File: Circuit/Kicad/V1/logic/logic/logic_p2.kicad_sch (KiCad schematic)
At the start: 2 parts

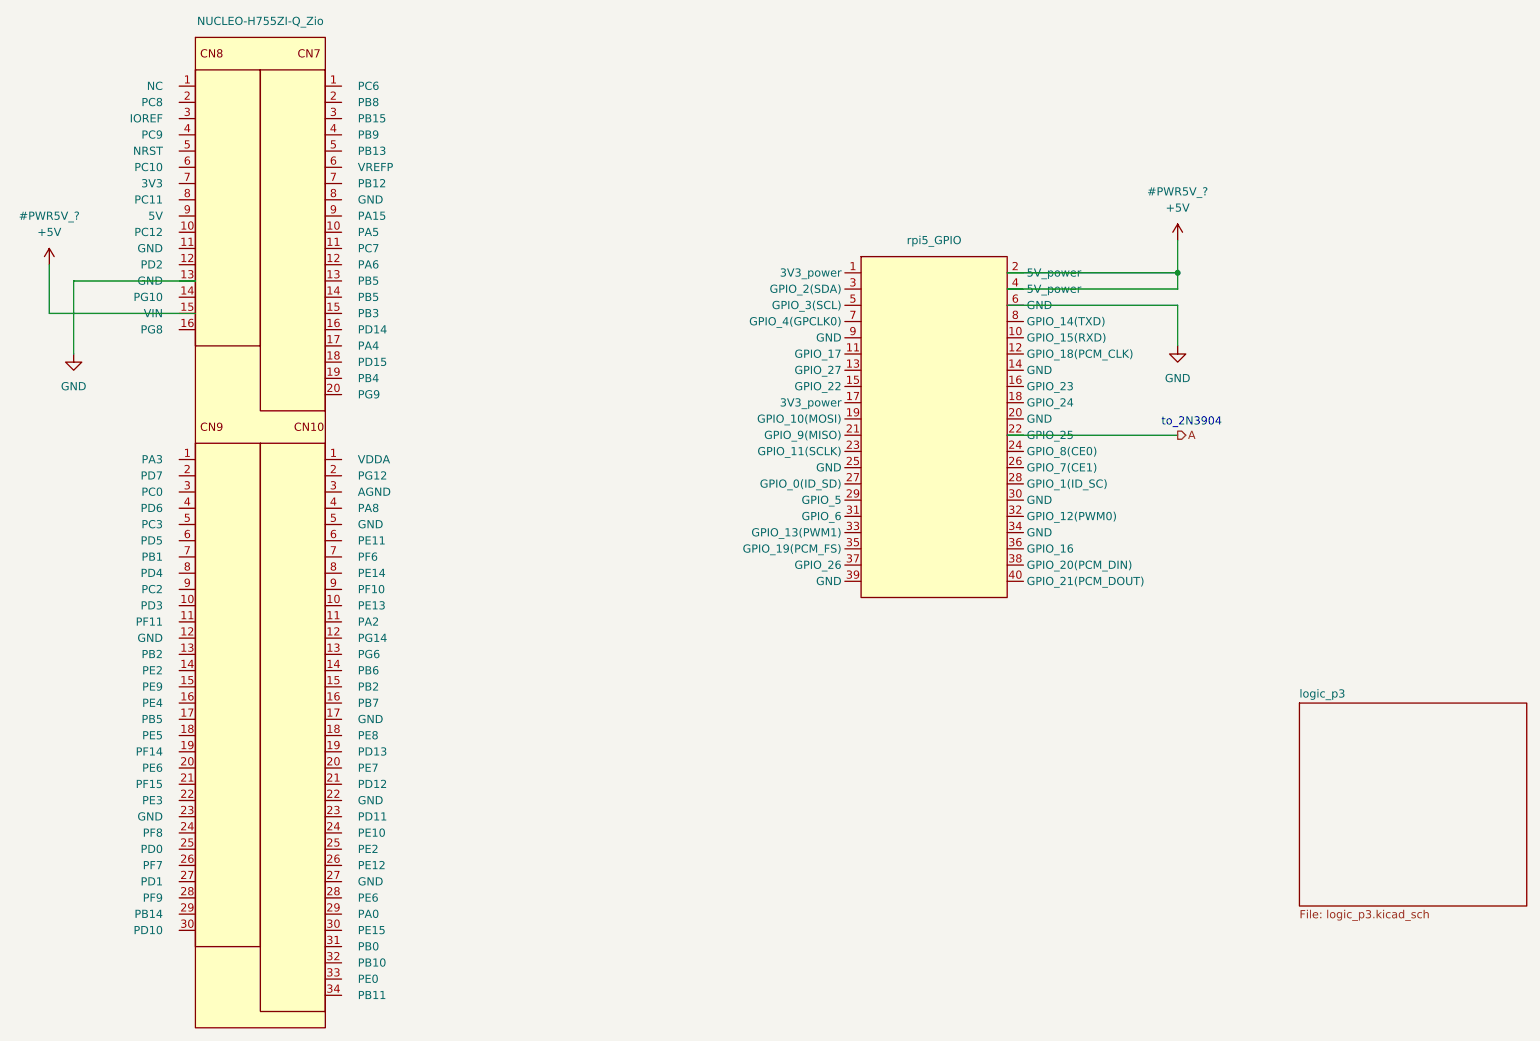
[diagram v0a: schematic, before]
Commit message: version1.2.1のLogic周りの回路図を書いた
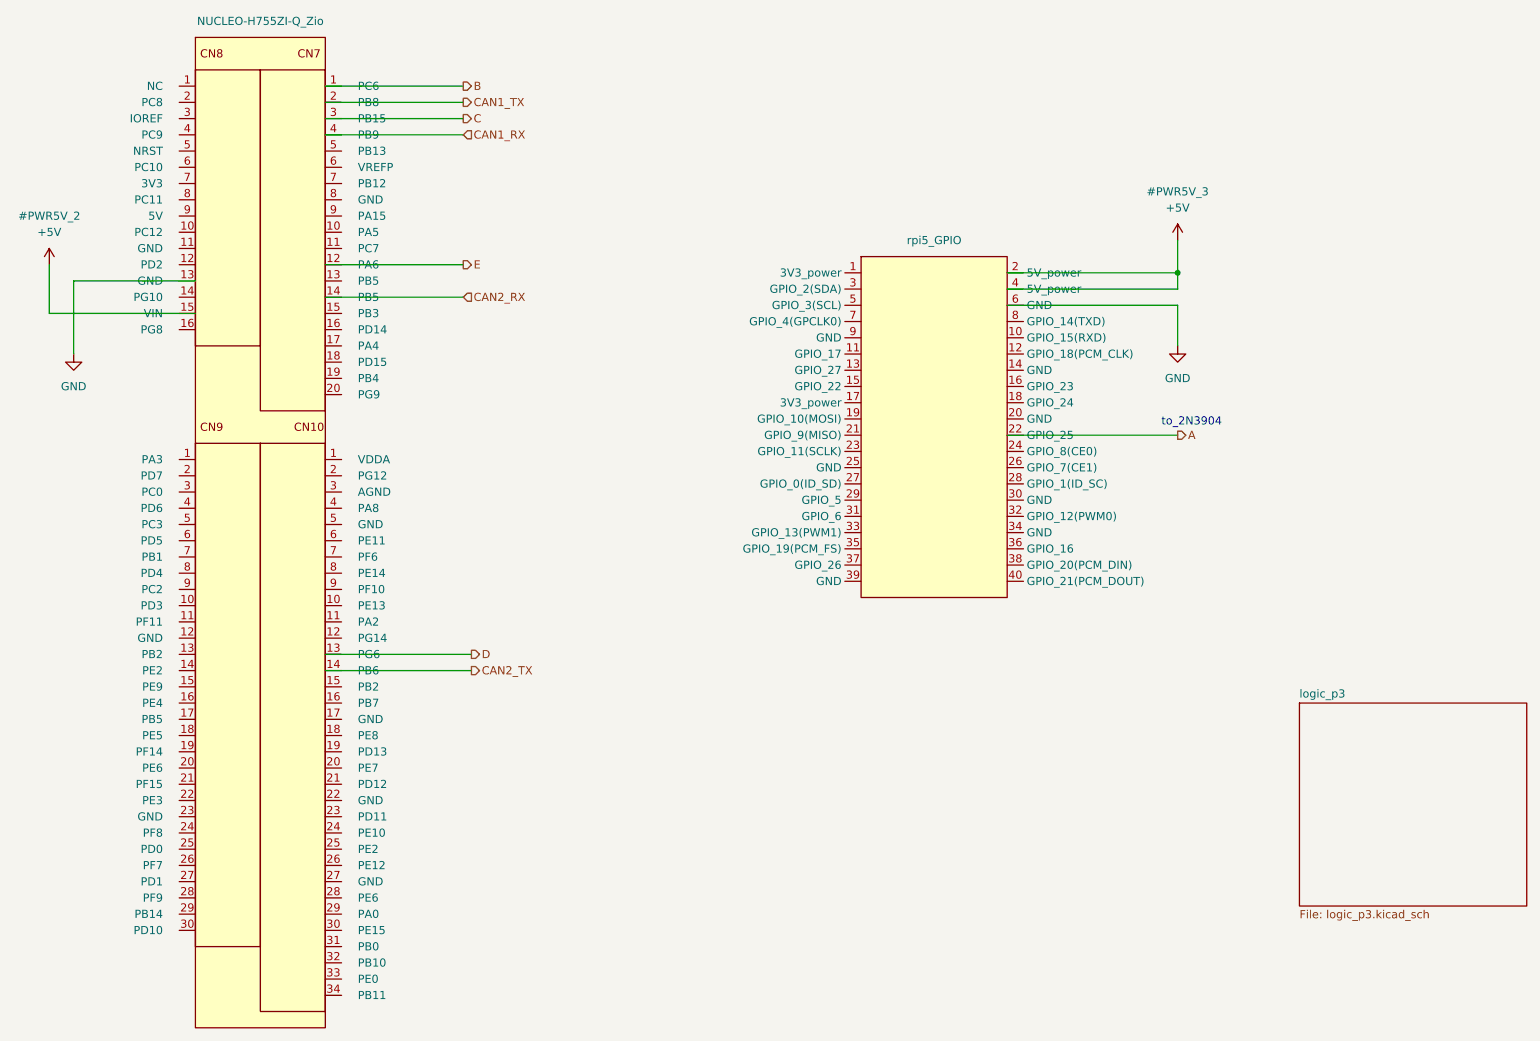
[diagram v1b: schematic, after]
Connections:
- net B: now reaches U?.1 (VDDA)
- net E: now reaches U?.12 (PG14)
- net CAN2_TX: now reaches U?.14 (PG10)
- net CAN1_TX: now reaches U?.2 (PG12)
- net C: now reaches U?.3 (PC0)
- net CAN1_RX: now reaches U?.4 (PD6)
- new net CAN2_RX: U?.14 (PG10)
- new net D: U?.13 (PG6)
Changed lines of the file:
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@@
+    (stroke (width 0) (type default) (color 0 0 0 0))
+  )
+  (wire (pts (xy 87.63 59.69) (xy 109.22 59.69))
     (stroke (width 0) (type default) (color 0 0 0 0))
   )
@@
     (stroke (width 0) (type default) (color 0 0 0 0))
   )
+  (wire (pts (xy 87.63 34.29) (xy 109.22 34.29))
+    (stroke (width 0) (type default) (color 0 0 0 0))
+  )
   (wire (pts (xy 220.98 63.5) (xy 220.98 60.96))
     (stroke (width 0) (type default) (color 0 0 0 0))
   )
+  (wire (pts (xy 87.63 120.65) (xy 110.49 120.65))
+    (stroke (width 0) (type default) (color 0 0 0 0))
+  )
   (wire (pts (xy 194.31 66.04) (xy 220.98 66.04))
     (stroke (width 0) (type default) (color 0 0 0 0))
   )
+  (wire (pts (xy 87.63 64.77) (xy 109.22 64.77))
+    (stroke (width 0) (type default) (color 0 0 0 0))
+  )
+  (wire (pts (xy 87.63 36.83) (xy 109.22 36.83))
+    (stroke (width 0) (type default) (color 0 0 0 0))
+  )
   (wire (pts (xy 67.31 67.31) (xy 44.45 67.31))
     (stroke (width 0) (type default) (color 0 0 0 0))
@@
     (stroke (width 0) (type default) (color 0 0 0 0))
   )
+  (wire (pts (xy 87.63 39.37) (xy 109.22 39.37))
+    (stroke (width 0) (type default) (color 0 0 0 0))
+  )
+  (wire (pts (xy 87.63 123.19) (xy 110.49 123.19))
+    (stroke (width 0) (type default) (color 0 0 0 0))
+  )
   (wire (pts (xy 48.26 62.23) (xy 48.26 73.66))
     (stroke (width 0) (type default) (color 0 0 0 0))
@@
   )
   (wire (pts (xy 220.98 60.96) (xy 194.31 60.96))
+    (stroke (width 0) (type default) (color 0 0 0 0))
+  )
+  (wire (pts (xy 87.63 31.75) (xy 109.22 31.75))
     (stroke (width 0) (type default) (color 0 0 0 0))
   )
@@
     (effects (font (size 1.27 1.27)) (justify left bottom))
   )
+  (hierarchical_label "D" (shape output) (at 110.49 120.65 0)
+    (effects (font (size 1.27 1.27)) (justify left))
+  )
+  (hierarchical_label "B" (shape output) (at 109.22 31.75 0)
+    (effects (font (size 1.27 1.27)) (justify left))
+  )
+  (hierarchical_label "CAN1_TX" (shape output) (at 109.22 34.29 0)
+    (effects (font (size 1.27 1.27)) (justify left))
+  )
+  (hierarchical_label "CAN1_RX" (shape input) (at 109.22 39.37 0)
+    (effects (font (size 1.27 1.27)) (justify left))
+  )
+  (hierarchical_label "CAN2_RX" (shape input) (at 109.22 64.77 0)
+    (effects (font (size 1.27 1.27)) (justify left))
+  )
+  (hierarchical_label "C" (shape output) (at 109.22 36.83 0)
+    (effects (font (size 1.27 1.27)) (justify left))
+  )
+  (hierarchical_label "E" (shape output) (at 109.22 59.69 0)
+    (effects (font (size 1.27 1.27)) (justify left))
+  )
   (hierarchical_label "A" (shape output) (at 220.98 86.36 0)
+    (effects (font (size 1.27 1.27)) (justify left))
+  )
+  (hierarchical_label "CAN2_TX" (shape output) (at 110.49 123.19 0)
     (effects (font (size 1.27 1.27)) (justify left))
   )
@@
   (symbol (lib_id "power:+5V") (at 44.45 59.69 0) (unit 1)
     (in_bom yes) (on_board yes)
-    (property "Reference" "#PWR5V_?" (id 0) (at 44.45 52.07 0))
+    (property "Reference" "#PWR5V_2" (id 0) (at 44.45 52.07 0))
     (property "Value" "+5V" (id 1) (at 44.45 54.61 0))
     (property "Footprint" "" (id 2) (at 44.45 59.69 0)
@@
   (symbol (lib_id "power:+5V") (at 220.98 55.88 0) (unit 1)
     (in_bom yes) (on_board yes)
-    (property "Reference" "#PWR5V_?" (id 0) (at 220.98 48.26 0))
+    (property "Reference" "#PWR5V_3" (id 0) (at 220.98 48.26 0))
     (property "Value" "+5V" (id 1) (at 220.98 50.8 0))
     (property "Footprint" "" (id 2) (at 220.98 55.88 0)
